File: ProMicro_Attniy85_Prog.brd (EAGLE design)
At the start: 31.7 x 21.6 mm, 4 parts, among them U1 ATTINY85-20P

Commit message: Add files via upload
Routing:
- net GND: track 44.7 -> 47.0 mm
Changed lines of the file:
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@@
 <wire x1="22.86" y1="17.78" x2="20.32" y2="15.24" width="0.4064" layer="1"/>
 <wire x1="20.32" y1="12.446" x2="20.32" y2="15.24" width="0.4064" layer="1"/>
-<wire x1="20.32" y1="12.446" x2="20.574" y2="12.446" width="0.2032" layer="1"/>
 <wire x1="5.08" y1="15.24" x2="7.874" y2="12.446" width="0.4064" layer="1"/>
 <wire x1="7.874" y1="12.446" x2="20.32" y2="12.446" width="0.4064" layer="1"/>
@@
 <contactref element="JP3" pad="21"/>
 <contactref element="JP3" pad="22"/>
+<wire x1="27.94" y1="2.54" x2="27.94" y2="5.08" width="0.4064" layer="1"/>
 </signal>
 <signal name="VCC">
@@
 <signal name="RST">
 <contactref element="C1" pad="2"/>
-<wire x1="25.4" y1="5.08" x2="25.4" y2="5.334" width="0.2032" layer="1"/>
 <wire x1="20.32" y1="10.414" x2="23.876" y2="10.414" width="0.2032" layer="1"/>
 <wire x1="25.4" y1="8.89" x2="25.4" y2="5.08" width="0.2032" layer="1"/>

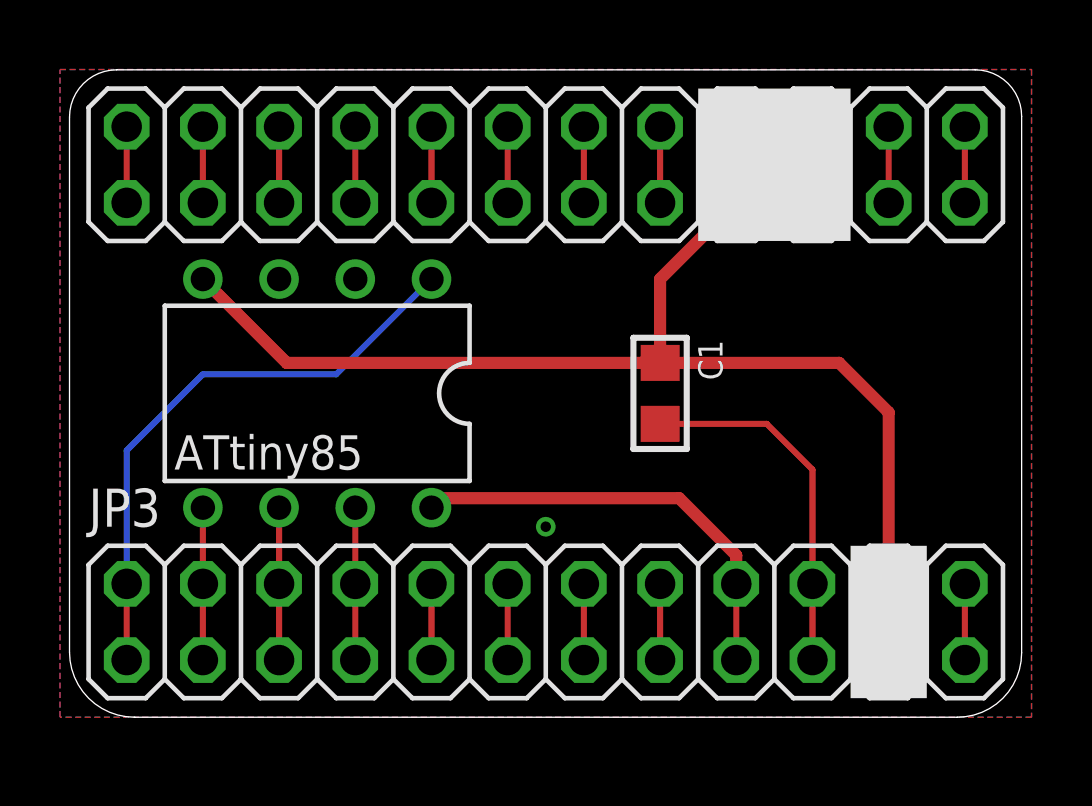
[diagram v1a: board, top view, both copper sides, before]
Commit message: Add files via upload
LEDs added following the desing in [Utiliza tu placa Arduino como programador para ATtiny]https://fabricadigital.org/tutoriales/utiliza-tu-placa-arduino-como-programador-para-attiny/
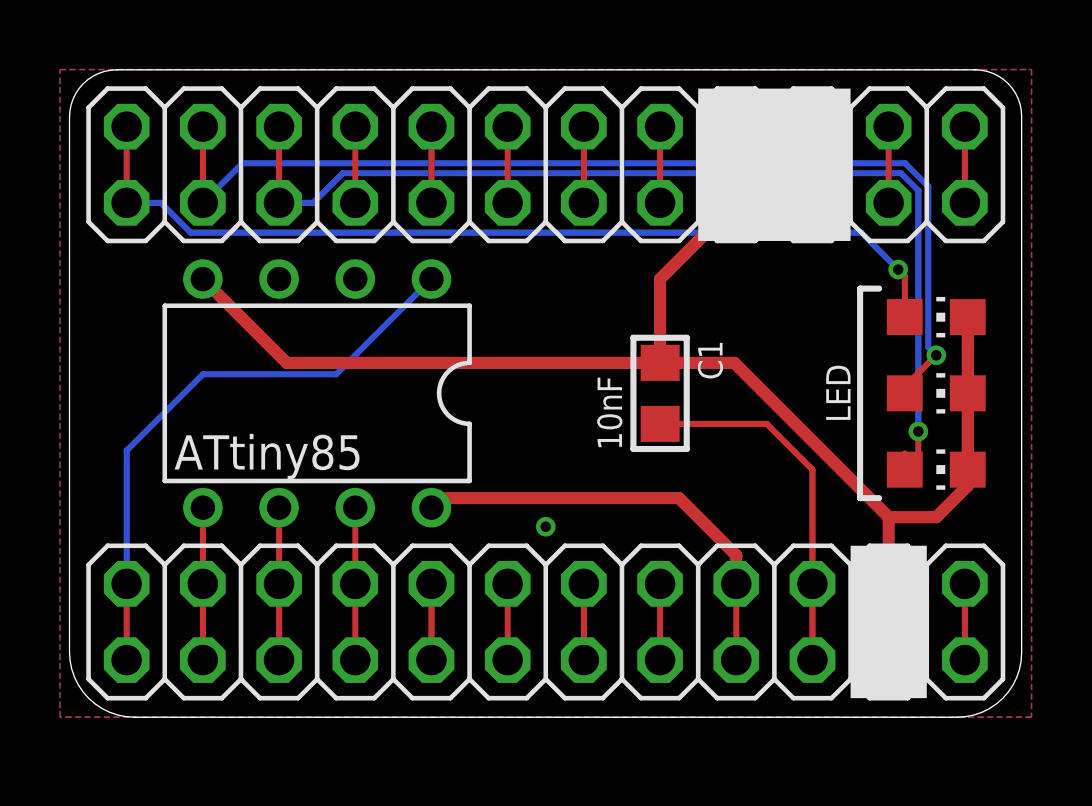
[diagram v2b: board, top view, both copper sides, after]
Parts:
- added LED1, LED2, LED3: (no value), led:CHIP-LED0805
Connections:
- removed net N$10: JP2.23, JP2.24
- removed net N$8: JP2.19, JP2.20
- removed net N$9: JP2.21, JP2.22
- new net PIN7: JP2.19, JP2.20, LED3.A
- new net PIN8: JP2.21, JP2.22, LED2.A
- new net PIN9: JP2.23, JP2.24, LED1.A
- net GND: now also LED1.C, LED2.C, LED3.C
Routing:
- net PIN8: track 0.00 -> 35.0 mm, vias 0 -> 1
- net PIN7: track 0.00 -> 34.5 mm, vias 0 -> 1
- net PIN9: track 0.00 -> 30.9 mm, vias 0 -> 1
- net GND: track 47.0 -> 53.6 mm
- net N$9: track 2.54 -> 0.00 mm
- net N$8: track 2.54 -> 0.00 mm
- net N$10: track 2.54 -> 0.00 mm
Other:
- board text added: "10nF"
- board text added: "LED"
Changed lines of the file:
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@@
 <rectangle x1="21.59" y1="16.51" x2="26.67" y2="21.59" layer="21"/>
 <rectangle x1="26.67" y1="1.27" x2="29.21" y2="6.35" layer="21"/>
+<wire x1="27.6225" y1="14.9225" x2="26.9875" y2="14.9225" width="0.2032" layer="21"/>
+<wire x1="26.9875" y1="14.9225" x2="26.9875" y2="7.9375" width="0.2032" layer="21"/>
+<wire x1="26.9875" y1="7.9375" x2="27.6225" y2="7.9375" width="0.2032" layer="21"/>
+<text x="19.05" y="9.525" size="0.8128" layer="21" rot="R90">10nF</text>
+<text x="26.67" y="11.43" size="0.8128" layer="21" rot="R90" align="bottom-center">LED</text>
 </plain>
 <attributes>
@@
 </element>
 <element name="JP3" library="pinhead" library_urn="urn:adsk.eagle:library:325" package="2X12" package3d_urn="urn:adsk.eagle:package:22420/2" value="" x="16.51" y="3.81" smashed="yes">
-<attribute name="NAME" x="1.27" y="6.985" size="1.27" layer="25" ratio="10"/>
 <attribute name="VALUE" x="1.27" y="-0.635" size="1.27" layer="27"/>
+</element>
+<element name="LED1" library="led" library_urn="urn:adsk.eagle:library:259" package="CHIP-LED0805" package3d_urn="urn:adsk.eagle:package:15818/2" value="" x="29.5275" y="13.97" smashed="yes" rot="R270">
+<attribute name="VALUE" x="28.2575" y="11.43" size="1.27" layer="27"/>
+</element>
+<element name="LED2" library="led" library_urn="urn:adsk.eagle:library:259" package="CHIP-LED0805" package3d_urn="urn:adsk.eagle:package:15818/2" value="" x="29.5275" y="11.43" smashed="yes" rot="R270">
+<attribute name="VALUE" x="28.2575" y="8.89" size="1.27" layer="27"/>
+</element>
+<element name="LED3" library="led" library_urn="urn:adsk.eagle:library:259" package="CHIP-LED0805" package3d_urn="urn:adsk.eagle:package:15818/2" value="" x="29.5275" y="8.89" smashed="yes" rot="R270">
+<attribute name="VALUE" x="28.2575" y="6.35" size="1.27" layer="27"/>
 </element>
 </elements>
@@
 <wire x1="5.08" y1="15.24" x2="7.874" y2="12.446" width="0.4064" layer="1"/>
 <wire x1="7.874" y1="12.446" x2="20.32" y2="12.446" width="0.4064" layer="1"/>
-<wire x1="20.32" y1="12.446" x2="26.289" y2="12.446" width="0.4064" layer="1"/>
-<wire x1="27.94" y1="10.795" x2="27.94" y2="5.08" width="0.4064" layer="1"/>
-<wire x1="26.289" y1="12.446" x2="27.94" y2="10.795" width="0.4064" layer="1"/>
+<wire x1="20.32" y1="12.446" x2="22.7965" y2="12.446" width="0.4064" layer="1"/>
+<wire x1="27.94" y1="5.08" x2="27.94" y2="7.3025" width="0.4064" layer="1"/>
+<wire x1="22.7965" y1="12.446" x2="27.94" y2="7.3025" width="0.4064" layer="1"/>
 <wire x1="22.86" y1="20.32" x2="25.4" y2="20.32" width="0.4064" layer="1"/>
 <polygon width="0.1524" layer="16">
@@
 <contactref element="JP3" pad="22"/>
 <wire x1="27.94" y1="2.54" x2="27.94" y2="5.08" width="0.4064" layer="1"/>
+<contactref element="LED1" pad="C"/>
+<contactref element="LED2" pad="C"/>
+<contactref element="LED3" pad="C"/>
+<wire x1="30.5775" y1="13.97" x2="30.5775" y2="11.43" width="0.4064" layer="1"/>
+<wire x1="30.5775" y1="11.43" x2="30.5775" y2="8.89" width="0.4064" layer="1"/>
+<wire x1="27.94" y1="7.3025" x2="29.5275" y2="7.3025" width="0.4064" layer="1"/>
+<wire x1="29.5275" y1="7.3025" x2="30.5775" y2="8.3525" width="0.4064" layer="1"/>
+<wire x1="30.5775" y1="8.3525" x2="30.5775" y2="8.89" width="0.4064" layer="1"/>
 </signal>
 <signal name="VCC">
@@
 <wire x1="10.16" y1="17.78" x2="10.16" y2="20.32" width="0.2032" layer="1"/>
 </signal>
-<signal name="N$8">
+<signal name="PIN7">
 <contactref element="JP2" pad="19"/>
 <contactref element="JP2" pad="20"/>
 <wire x1="7.62" y1="17.78" x2="7.62" y2="20.32" width="0.2032" layer="1"/>
-</signal>
-<signal name="N$9">
+<contactref element="LED3" pad="A"/>
+<wire x1="7.62" y1="17.78" x2="8.759075" y2="17.78" width="0.2032" layer="16"/>
+<wire x1="8.759075" y1="17.78" x2="9.749675" y2="18.7706" width="0.2032" layer="16"/>
+<wire x1="28.4775" y1="9.4275" x2="28.4775" y2="8.89" width="0.2032" layer="1"/>
+<wire x1="9.749675" y1="18.7706" x2="28.350325" y2="18.7706" width="0.2032" layer="16"/>
+<wire x1="28.350325" y1="18.7706" x2="28.9306" y2="18.190325" width="0.2032" layer="16"/>
+<via x="28.9306" y="10.16" extent="1-16" drill="0.35"/>
+<wire x1="28.9306" y1="10.16" x2="28.9306" y2="9.3431" width="0.2032" layer="1"/>
+<wire x1="28.9306" y1="9.3431" x2="28.4775" y2="8.89" width="0.2032" layer="1"/>
+<wire x1="28.9306" y1="18.190325" x2="28.9306" y2="10.16" width="0.2032" layer="16"/>
+</signal>
+<signal name="PIN8">
 <contactref element="JP2" pad="21"/>
 <contactref element="JP2" pad="22"/>
 <wire x1="5.08" y1="17.78" x2="5.08" y2="20.32" width="0.2032" layer="1"/>
-</signal>
-<signal name="N$10">
+<contactref element="LED2" pad="A"/>
+<wire x1="5.08" y1="17.78" x2="6.4008" y2="19.1008" width="0.2032" layer="16"/>
+<wire x1="28.4871" y1="19.1008" x2="29.2608" y2="18.3271" width="0.2032" layer="16"/>
+<wire x1="29.2608" y1="12.9667" x2="29.5275" y2="12.7" width="0.2032" layer="16"/>
+<via x="29.5275" y="12.7" extent="1-16" drill="0.35"/>
+<wire x1="29.5275" y1="12.7" x2="28.4775" y2="11.65" width="0.2032" layer="1"/>
+<wire x1="28.4775" y1="11.65" x2="28.4775" y2="11.43" width="0.2032" layer="1"/>
+<wire x1="6.4008" y1="19.1008" x2="28.4871" y2="19.1008" width="0.2032" layer="16"/>
+<wire x1="29.2608" y1="18.3271" x2="29.2608" y2="12.9667" width="0.2032" layer="16"/>
+</signal>
+<signal name="PIN9">
 <contactref element="JP2" pad="23"/>
 <contactref element="JP2" pad="24"/>
 <wire x1="2.54" y1="20.32" x2="2.54" y2="17.78" width="0.2032" layer="1"/>
+<contactref element="LED1" pad="A"/>
+<wire x1="2.54" y1="17.78" x2="3.679075" y2="17.78" width="0.2032" layer="16"/>
+<wire x1="3.679075" y1="17.78" x2="4.669675" y2="16.7894" width="0.2032" layer="16"/>
+<wire x1="27.0256" y1="16.7894" x2="28.2575" y2="15.5575" width="0.2032" layer="16"/>
+<via x="28.2575" y="15.5575" extent="1-16" drill="0.35"/>
+<wire x1="28.2575" y1="15.5575" x2="28.4775" y2="15.3375" width="0.2032" layer="1"/>
+<wire x1="28.4775" y1="15.3375" x2="28.4775" y2="13.97" width="0.2032" layer="1"/>
+<wire x1="4.669675" y1="16.7894" x2="27.0256" y2="16.7894" width="0.2032" layer="16"/>
 </signal>
 <signal name="N$11">

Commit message: Add files via upload
minor changes
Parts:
- added R1, R2, R3: (no value), rc-master-smd:R0805
- moved LED1 5.08 mm to (24.4, 14.0), turned to 90 degrees
- moved LED2 5.08 mm to (24.4, 11.4), turned to 90 degrees
- moved LED3 5.08 mm to (24.4, 8.89), turned to 90 degrees
- moved C1 1.91 mm to (18.4, 11.4)
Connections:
- new net N$10: LED1.A, R3.2
- new net N$8: LED3.A, R1.2
- new net N$9: LED2.A, R2.2
- net PIN7: now also R1.1; no longer LED3.A
- net PIN8: now also R2.1; no longer LED2.A
- net PIN9: now also R3.1; no longer LED1.A
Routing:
- net GND: track 53.6 -> 44.6 mm
- net N$9: track 0.00 -> 2.70 mm
- net N$8: track 0.00 -> 2.70 mm
- net N$10: track 0.00 -> 2.70 mm
- net PIN8: track 35.0 -> 37.1 mm
- net PIN7: track 34.5 -> 36.5 mm
- net PIN9: track 30.9 -> 32.5 mm
